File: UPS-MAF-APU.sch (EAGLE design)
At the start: 7 parts, among them IC1 M24C32-RDW6TP, IC2 INA260AIPW, IC3 OKI-78SR-5_1.5-W36H-C, J1 CONNECTOR_PI_40_PIN, J2 PJ-102AH, J3 CONNECTOR_4, U1 OLED_I2C

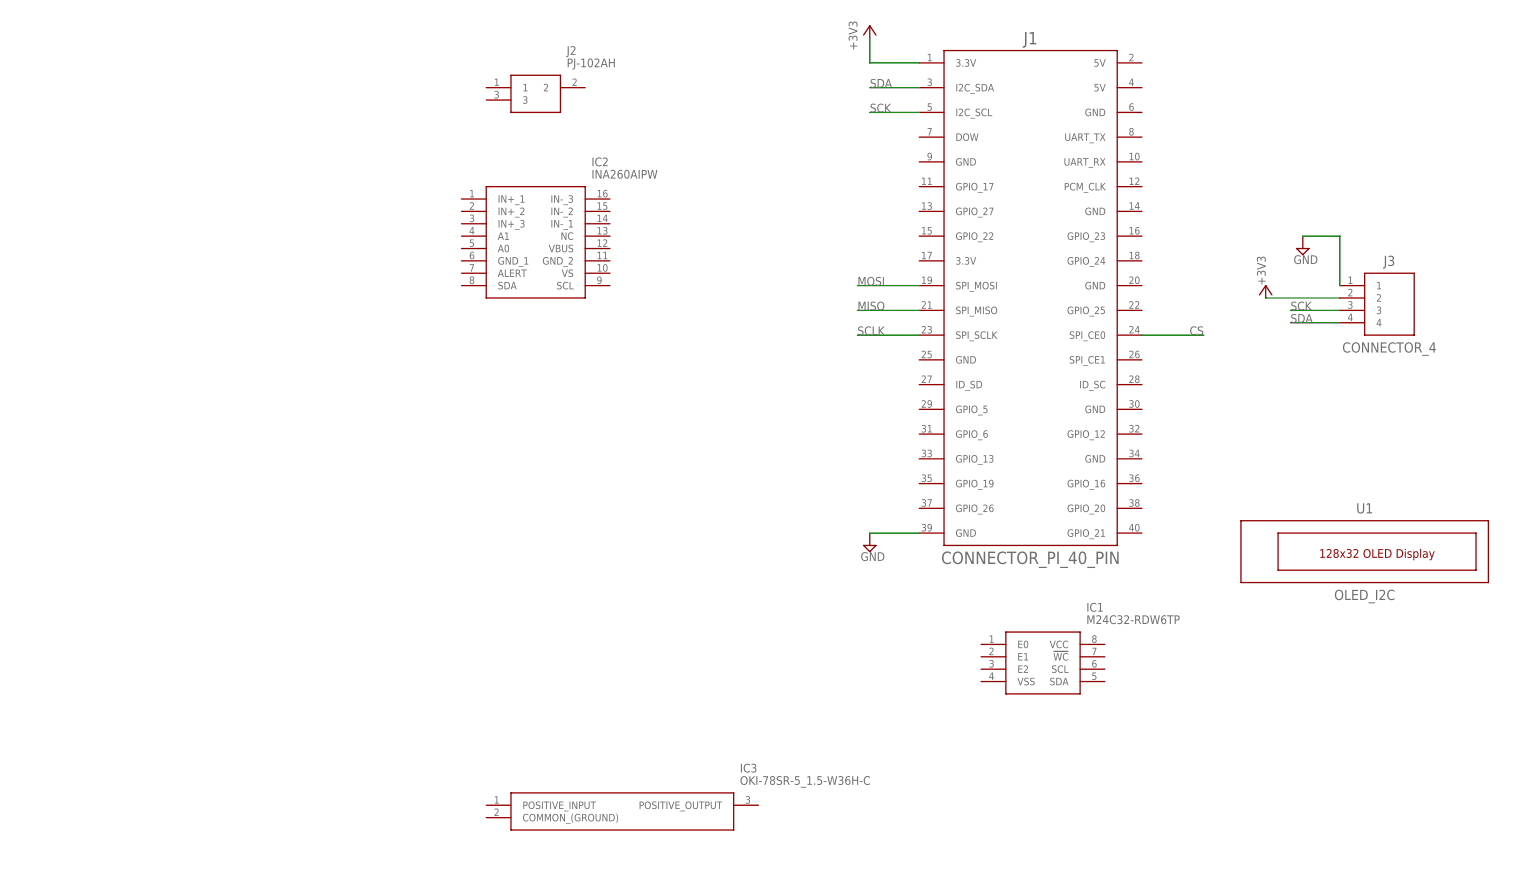
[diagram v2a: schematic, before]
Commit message: Add tons of parts to Library and Schematic, update symbol styles.
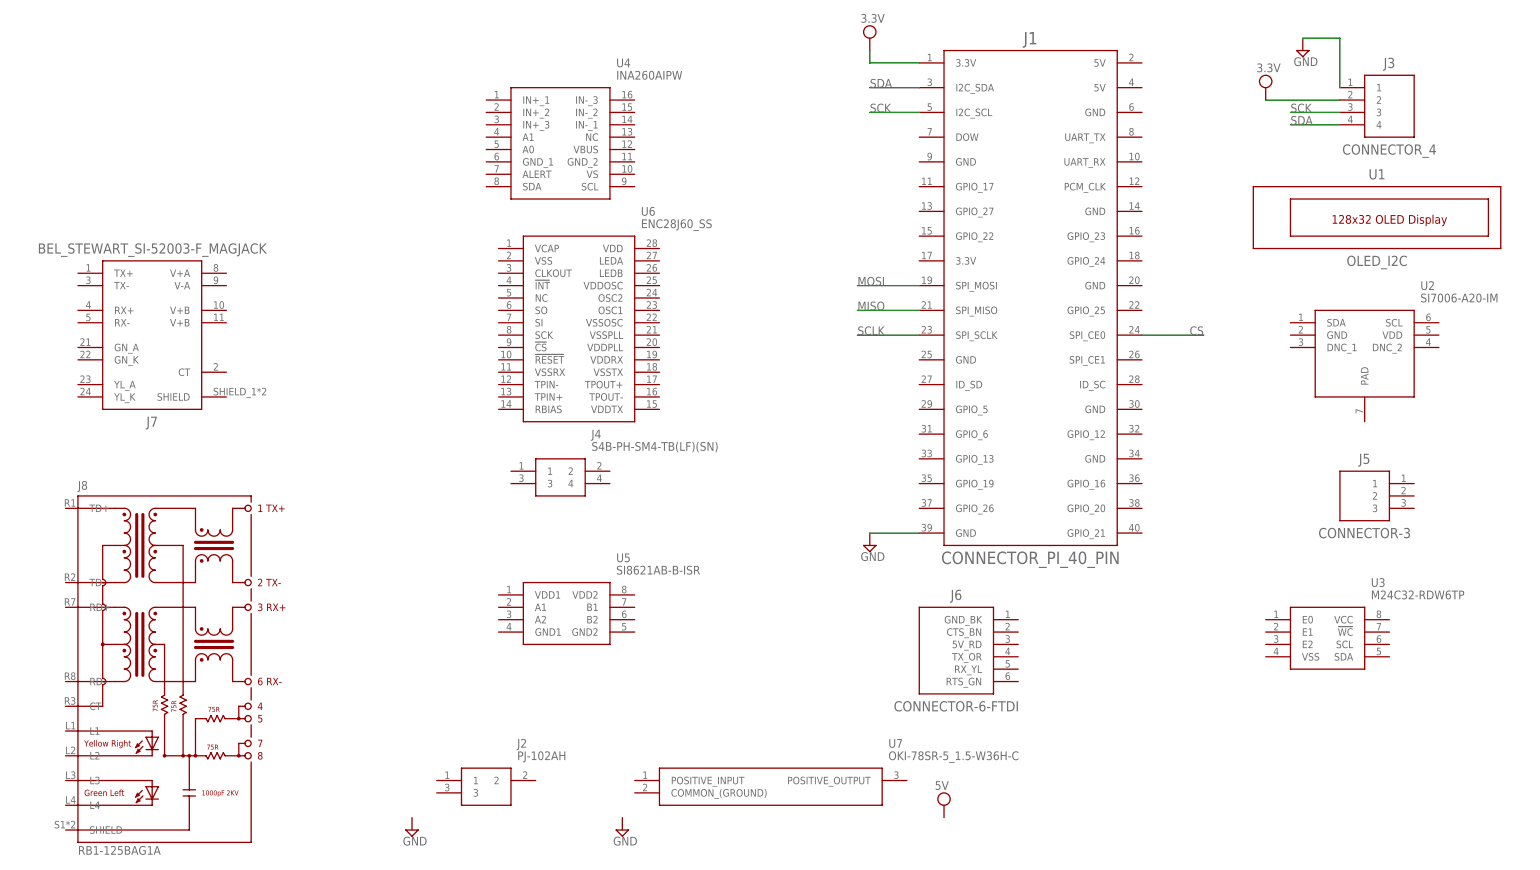
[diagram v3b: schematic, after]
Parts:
- removed IC1: M24C32-RDW6TP, APU_ENGR480_UPS_EAGLE_Library:M24C32-RDW6TP
- removed IC2: INA260AIPW, APU_ENGR480_UPS_EAGLE_Library:INA260AIPW
- removed IC3: OKI-78SR-5_1.5-W36H-C, APU_ENGR480_UPS_EAGLE_Library:OKI-78SR-5_1.5-W36H-C
- added J4: S4B-PH-SM4-TB(LF)(SN), APU_ENGR480_UPS_EAGLE_Library:S4B-PH-SM4-TB(LF)(SN)
- added J5: CONNECTOR-3, APU_ENGR480_UPS_EAGLE_Library:CONNECTOR-3
- added J6: CONNECTOR-6-FTDI, APU_ENGR480_UPS_EAGLE_Library:CONNECTOR-6-FTDI
- added J7: BEL_STEWART_SI-52003-F_MAGJACK, APU_ENGR480_UPS_EAGLE_Library:BEL_STEWART_SI-52003-F_MAGJACK
- added J8: RB1-125BAG1A, APU_ENGR480_UPS_EAGLE_Library:RB1-125BAG1A
- added U2: SI7006-A20-IM, APU_ENGR480_UPS_EAGLE_Library:SI7006-A20-IM
- added U3: M24C32-RDW6TP, APU_ENGR480_UPS_EAGLE_Library:M24C32-RDW6TP
- added U4: INA260AIPW, APU_ENGR480_UPS_EAGLE_Library:INA260AIPW
- added U5: SI8621AB-B-ISR, APU_ENGR480_UPS_EAGLE_Library:SI8621AB-B-ISR
- added U6: ENC28J60_SS, APU_ENGR480_UPS_EAGLE_Library:ENC28J60_SS
- added U7: OKI-78SR-5_1.5-W36H-C, APU_ENGR480_UPS_EAGLE_Library:OKI-78SR-5_1.5-W36H-C
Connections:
- net +3V3 renamed 3.3V
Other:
- note added: "add battery/charger connector pick which RJ-45 magjack add power, status lights"
- note removed: "add battery/charger connector add JST-4 for console add galvanic isolator add 1x6 for FTDI? add RJ-45 magjack add power LED add external temp connector add Si7006 internal temp/humidity add power, status lights"
- moved on the sheet: J2, J3, U1

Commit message: Add parts to schematic, change to Tabloid size page/frame.
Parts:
- removed J8: RB1-125BAG1A, APU_ENGR480_UPS_EAGLE_Library:RB1-125BAG1A
- J2: value PJ-102AH -> Barrel DC In
- J3: value CONNECTOR_4 -> OLED
- J4: value S4B-PH-SM4-TB(LF)(SN) -> VE.Direct Serial
- J5: value CONNECTOR-3 -> External DS18B20 Temp
- J6: value CONNECTOR-6-FTDI -> FTDI Serial Console
- J7: value BEL_STEWART_SI-52003-F_MAGJACK -> MagJack; device APU_ENGR480_UPS_EAGLE_Library:BEL_STEWART_SI-52003-F_MAGJACK -> APU_ENGR480_UPS_EAGLE_Library:RB1-125BAG1A
- U3: value M24C32-RDW6TP -> HAT EEPROM
- U5: value SI8621AB-B-ISR -> Isolator
- U7: value OKI-78SR-5_1.5-W36H-C -> 5V SMPS
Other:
- note added: "I2C Address 0x3C"
- note added: "I2C Address 0x??"
- note added: "add battery/charger connector add power, status lights"
- note removed: "add battery/charger connector pick which RJ-45 magjack add power, status lights"
- moved on the sheet: J2, J3, J4, J5, J6, U1, U2, U3, U4, U5, U6, U7

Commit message: SamChange
editpush?
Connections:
- new net BATTERY+: U4.IN-_1, U4.IN-_2, U4.IN-_3, U4.VBUS
- new net BATTERY-: U4.IN+_1, U4.IN+_2, U4.IN+_3
- new net N$1: J1.UART_TX@8, J6.TX_OR@4
- new net N$2: J1.UART_RX@10, J6.RX_YL@5
- new net N$4: J1.DOW@7, J5.2
- net 3.3V: now also J5.3, J6.5V_RD@3, U4.A0, U4.VS
- net GND: now also J5.1, J6.GND_BK@1, U4.A1, U4.GND_1, U4.GND_2
- net SCK: now also U2.SCL, U4.SCL
- net SDA: now also U2.SDA, U4.SDA
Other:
- moved on the sheet: J2, J5, J6, J7, U2, U4

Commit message: README
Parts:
- added Y1: ECS-250-20-3X-EN-TR, ECS-250-20-3X-EN-TR:ECS-250-20-3X-EN-TR
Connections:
- new net N$3: U6.TPIN+
- new net N$5: U6.TPIN-
- new net N$6: J7.TD-, U6.TPOUT-
- new net N$7: J7.TD+, U6.TPOUT+
- net 3.3V: now also U6.VDD, U6.VDDOSC, U6.VDDPLL, U6.VDDRX
- net GND: now also J7.SHIELD, U6.VSS, U6.VSSOSC, U6.VSSPLL, U6.VSSTX, U7.COMMON_(GROUND)
- net MISO: now also U6.SO
- net MOSI: now also U6.SI
- net SCLK: now also U6.SCK
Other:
- moved on the sheet: J2
